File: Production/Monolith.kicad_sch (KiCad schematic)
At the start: 0 parts

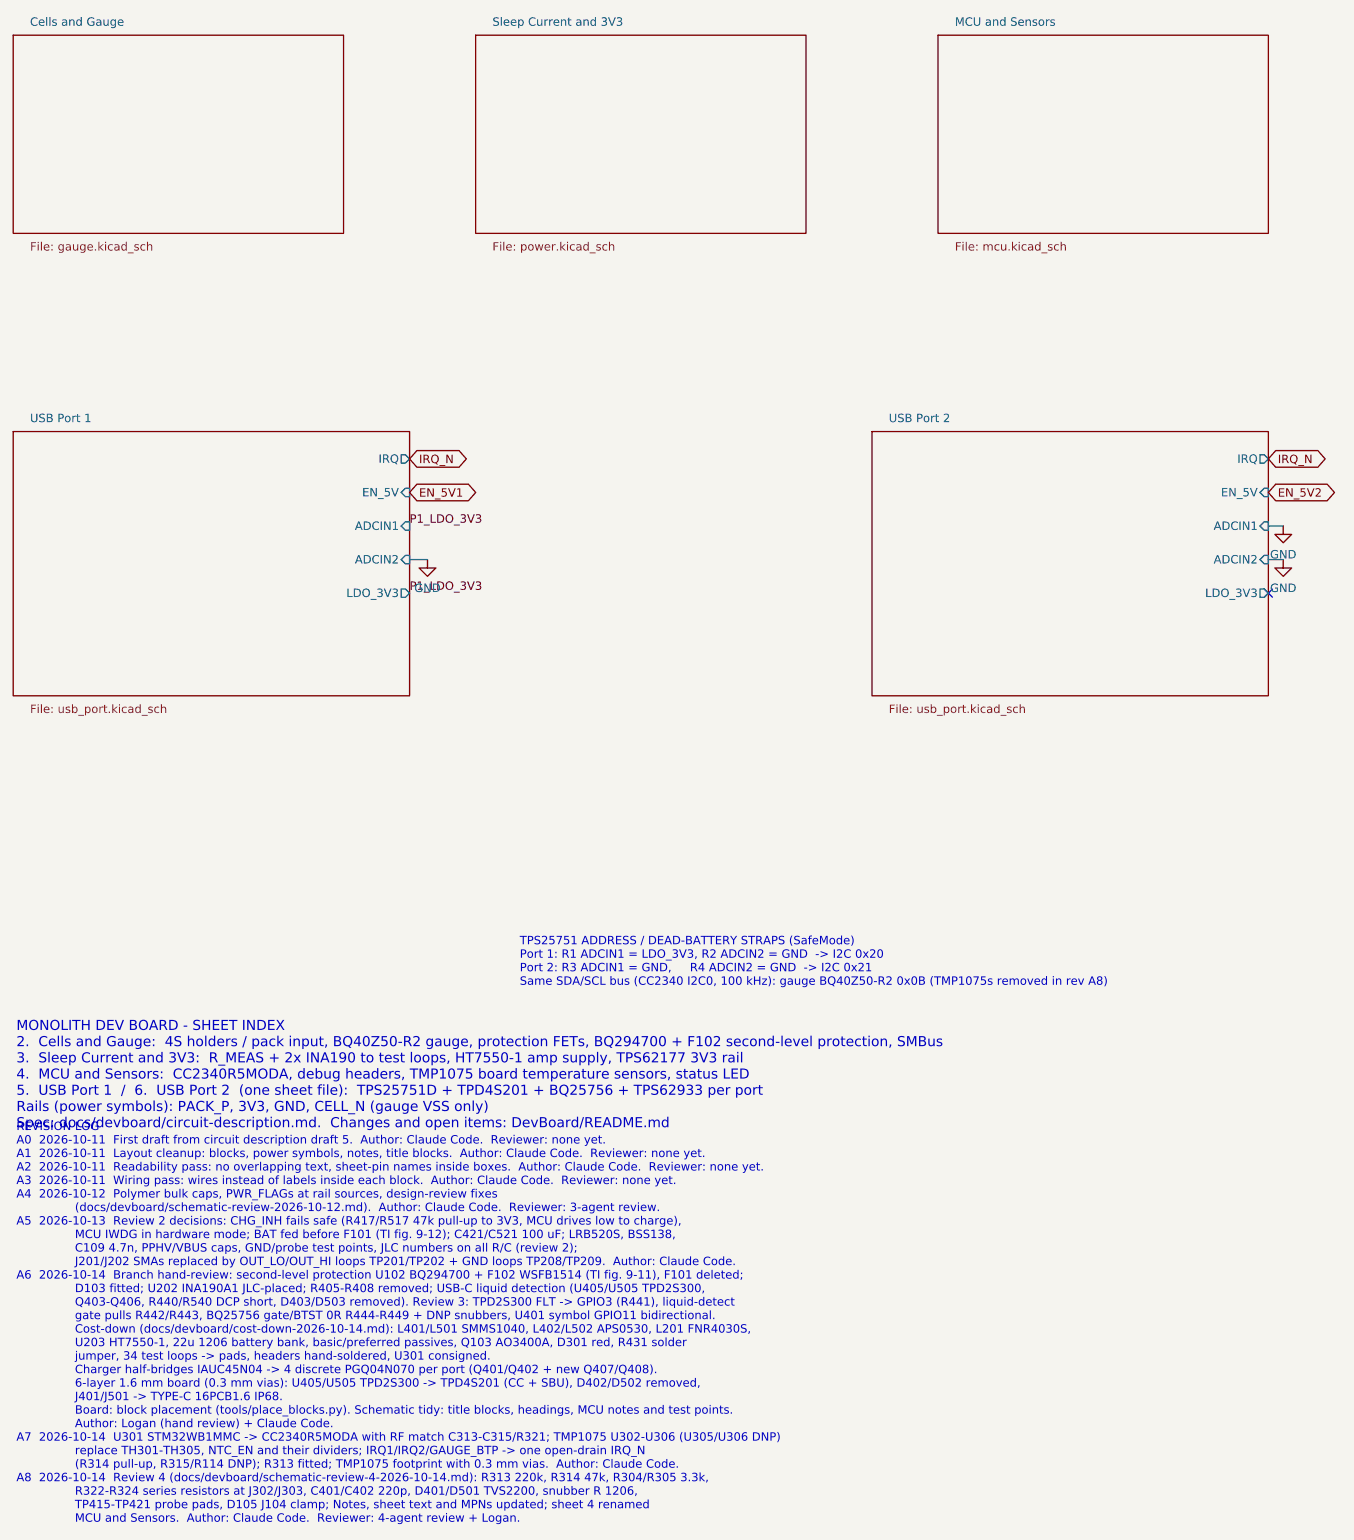
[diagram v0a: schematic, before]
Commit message: Production schematic P0: drawing tidy
tools/tidy_production.py (runs after make_production.py): pogo pads in their
own row, TC2030 under its SWD heading, link-merge leftovers removed, empty
headings deleted, sheet notes, root index and revision log rewritten for
production, sheets renamed 3V3 Rail and MCU. Netlist unchanged (check_netlist
passes); ERC: no errors.

Co-Authored-By: Claude Opus 5.5 <noreply@anthropic.com>
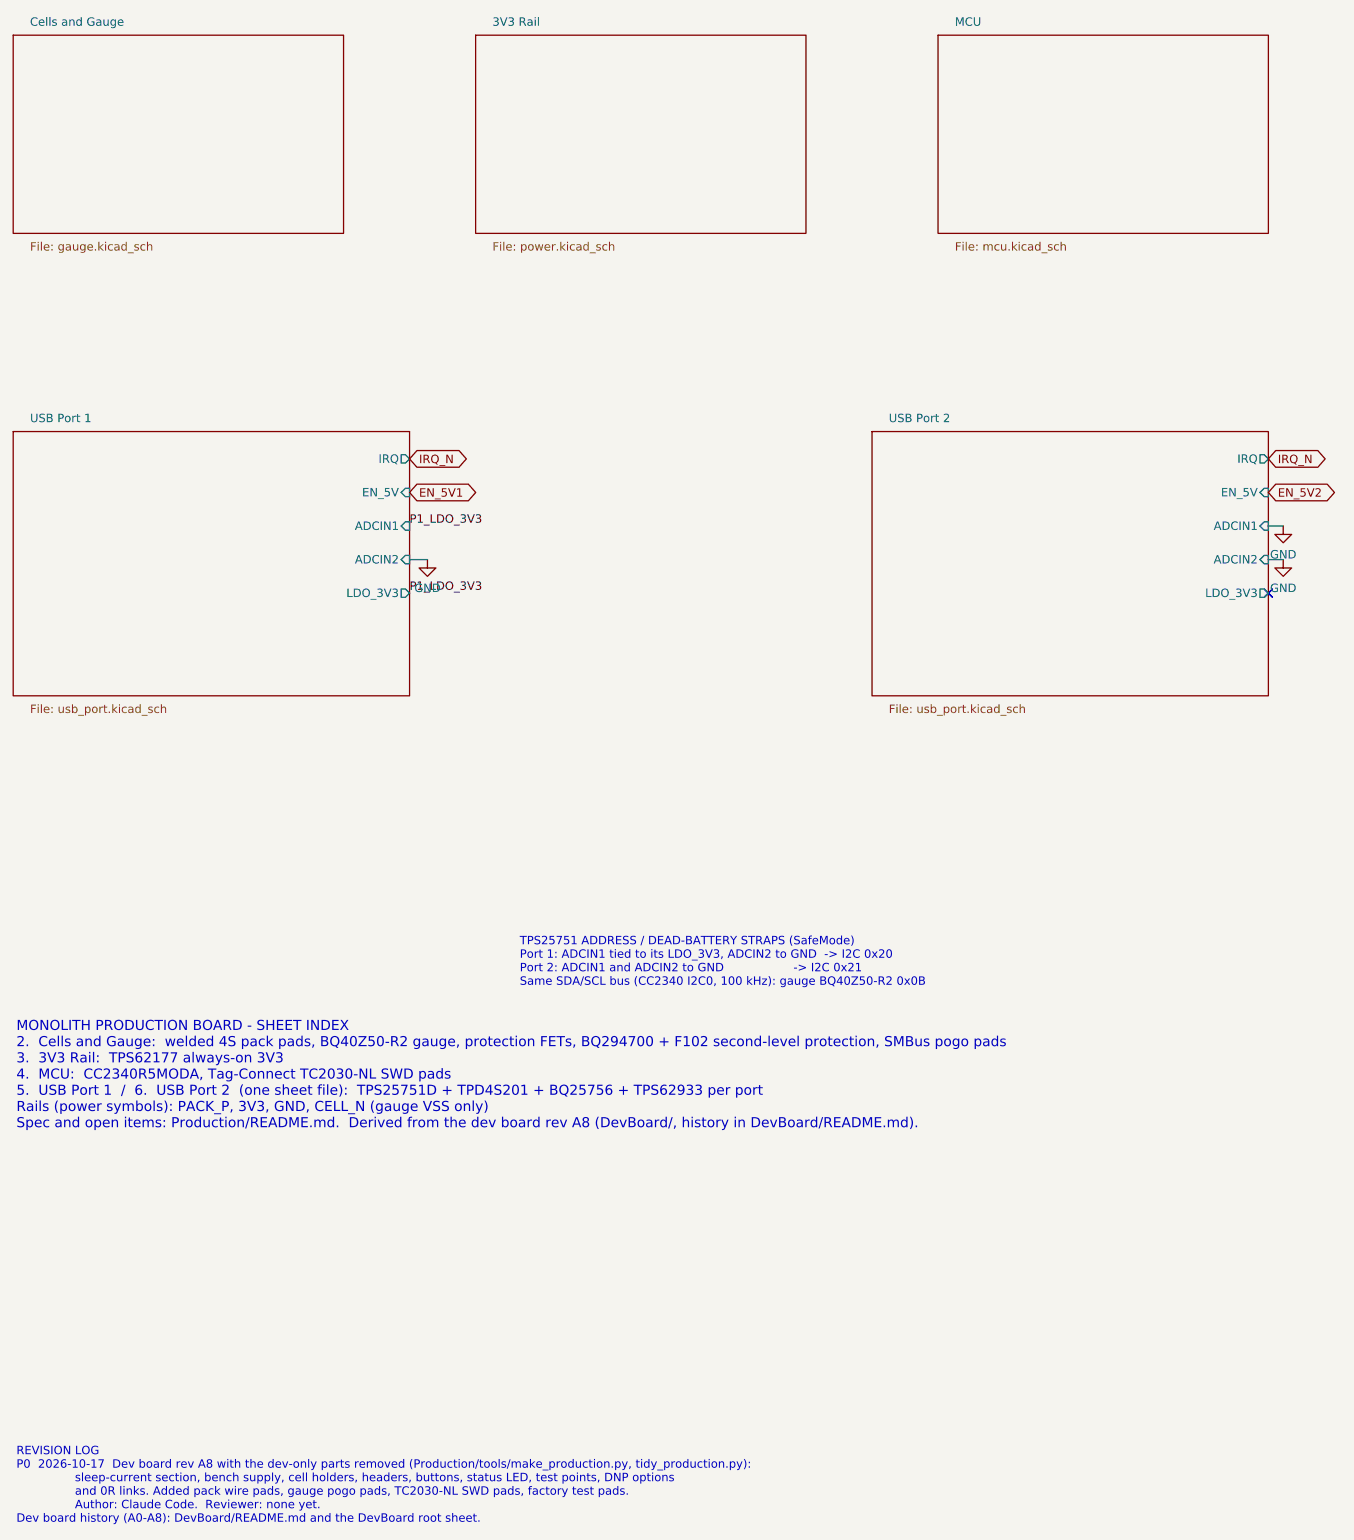
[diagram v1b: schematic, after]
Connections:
- no-connect marks 1 -> 2
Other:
- sheet MCU and Sensors renamed MCU
- sheet Sleep Current and 3V3 renamed 3V3 Rail
- note added: "MONOLITH PRODUCTION BOARD - SHEET INDEX 2. Cells and Gauge: welded 4S pack pads, BQ40Z50-R2 gauge, protection FETs, BQ294700 + F102 second-level protection, SMBus pogo pads 3. 3V3 Rail: TPS62177 always-on 3V3 4. MCU: CC2340R5MODA, Tag-Connect TC2030-NL SWD pads 5. USB Port 1 / 6. USB Port 2 (one sheet file): TPS25751D + TPD4S201 + BQ25756 + TPS62933 per port Rails (power symbols): PACK_P, 3V3, GN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"
- note added: "REVISION LOG P0 2026-10-17 Dev board rev A8 with the dev-only parts removed (Production/tools/make_production.py, tidy_production.py): sleep-current section, bench supply, cell holders, headers, buttons, status LED, test points, DNP options and 0R links. Added pack wire pads, gauge pogo pads, TC2030-NL SWD pads, factory test pads. Author: Claude Code. Reviewer: none yet. Dev board history (A0-A8)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"
- note added: "TPS25751 ADDRESS / DEAD-BATTERY STRAPS (SafeMode) Port 1: ADCIN1 tied to its LDO_3V3, ADCIN2 to GND -> I2C 0x20 Port 2: ADCIN1 and ADCIN2 to GND -> I2C 0x21 Same SDA/SCL bus (CC2340 I2C0, 100 kHz): gauge BQ40Z50-R2 0x0B"
- note removed: "MONOLITH DEV BOARD - SHEET INDEX 2. Cells and Gauge: 4S holders / pack input, BQ40Z50-R2 gauge, protection FETs, BQ294700 + F102 second-level protection, SMBus 3. Sleep Current and 3V3: R_MEAS + 2x INA190 to test loops, HT7550-1 amp supply, TPS62177 3V3 rail 4. MCU and Sensors: CC2340R5MODA, debug headers, TMP1075 board temperature sensors, status LED 5. USB Port 1 / 6. USB Port 2 (one sheet file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"
- note removed: "REVISION LOG A0 2026-10-11 First draft from circuit description draft 5. Author: Claude Code. Reviewer: none yet. A1 2026-10-11 Layout cleanup: blocks, power symbols, notes, title blocks. Author: Claude Code. Reviewer: none yet. A2 2026-10-11 Readability pass: no overlapping text, sheet-pin names inside boxes. Author: Claude Code. Reviewer: none yet. A3 2026-10-11 Wiring pass: wires instead of la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"
- note removed: "TPS25751 ADDRESS / DEAD-BATTERY STRAPS (SafeMode) Port 1: R1 ADCIN1 = LDO_3V3, R2 ADCIN2 = GND -> I2C 0x20 Port 2: R3 ADCIN1 = GND, R4 ADCIN2 = GND -> I2C 0x21 Same SDA/SCL bus (CC2340 I2C0, 100 kHz): gauge BQ40Z50-R2 0x0B (TMP1075s removed in rev A8)"
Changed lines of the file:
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@@
 		(company "Monolith 100 W battery bank - production")
 		(comment 1 "Sheet index, PD address straps")
-		(comment 2 "Spec + open items: DevBoard/README.md")
+		(comment 2 "Spec + open items: Production/README.md")
 		(comment 3 "P0: dev board rev A8 stripped by Production/tools/make_production.py; not reviewed")
 	)
-	(text "MONOLITH DEV BOARD - SHEET INDEX\n2.  Cells and Gauge:  4S holders / pack input, BQ40Z50-R2 gauge, protection FETs, BQ294700 + F102 second-level protection, SMBus\n3.  Sleep Current and 3V3:  R_MEAS + 2x INA190 to test loops, HT7550-1 amp supply, TPS62177 3V3 rail\n4.  MCU and Sensors:  CC2340R5MODA, debug headers, TMP1075 board temperature sensors, status LED\n5.  USB Port 1  /  6.  USB Port 2  (one sheet file):  TPS25751D + TPD4S201 + BQ25756 + TPS62933 per port\nRails (power symbols): PACK_P, 3V3, GND, CELL_N (gauge VSS only)\nSpec: docs/devboard/circuit-description.md.  Changes and open items: DevBoard/README.md"
+	(text "MONOLITH PRODUCTION BOARD - SHEET INDEX\n2.  Cells and Gauge:  welded 4S pack pads, BQ40Z50-R2 gauge, protection FETs, BQ294700 + F102 second-level protection, SMBus pogo pads\n3.  3V3 Rail:  TPS62177 always-on 3V3\n4.  MCU:  CC2340R5MODA, Tag-Connect TC2030-NL SWD pads\n5.  USB Port 1  /  6.  USB Port 2  (one sheet file):  TPS25751D + TPD4S201 + BQ25756 + TPS62933 per port\nRails (power symbols): PACK_P, 3V3, GND, CELL_N (gauge VSS only)\nSpec and open items: Production/README.md.  Derived from the dev board rev A8 (DevBoard/, history in DevBoard/README.md)."
 		(exclude_from_sim no)
 		(at 30.48 205.74 0)
@@
 		)
 	)
-	(text "REVISION LOG\nA0  2026-10-11  First draft from circuit description draft 5.  Author: Claude Code.  Reviewer: none yet.\nA1  2026-10-11  Layout cleanup: blocks, power symbols, notes, title blocks.  Author: Claude Code.  Reviewer: none yet.\nA2  2026-10-11  Readability pass: no overlapping text, sheet-pin names inside boxes.  Author: Claude Code.  Reviewer: none yet.\nA3  2026-10-11  Wiring pass: wires instead of labels inside each block.  Author: Claude Code.  Reviewer: none yet.\nA4  2026-10-12  Polymer bulk caps, PWR_FLAGs at rail sources, design-review fixes\n                (docs/devboard/schematic-review-2026-10-12.md).  Author: Claude Code.  Reviewer: 3-agent review.\nA5  2026-10-13  Review 2 decisions: CHG_INH fails safe (R417/R517 47k pull-up to 3V3, MCU drives low to charge),\n                MCU IWDG in hardware mode; BAT fed before F101 (TI fig. 9-12); C421/C521 100 uF; LRB520S, BSS138,\n                C109 4.7n, PPHV/VBUS caps, GND/probe test points, JLC numbers on all R/C (review 2);\n                J201/J202 SMAs replaced by OUT_LO/OUT_HI loops TP201/TP202 + GND loops TP208/TP209.  Author: Claude Code.\nA6  2026-10-14  Branch hand-review: second-level protection U102 BQ294700 + F102 WSFB1514 (TI fig. 9-11), F101 deleted;\n                D103 fitted; U202 INA190A1 JLC-placed; R405-R408 removed; USB-C liquid detection (U405/U505 TPD2S300,\n                Q403-Q406, R440/R540 DCP short, D403/D503 removed). Review 3: TPD2S300 FLT -> GPIO3 (R441), liquid-detect\n                gate pulls R442/R443, BQ25756 gate/BTST 0R R444-R449 + DNP snubbers, U401 symbol GPIO11 bidirectional.\n                Cost-down (docs/devboard/cost-down-2026-10-14.md): L401/L501 SMMS1040, L402/L502 APS0530, L201 FNR4030S,\n                U203 HT7550-1, 22u 1206 battery bank, basic/preferred passives, Q103 AO3400A, D301 red, R431 solder\n                jumper, 34 test loops -> pads, headers hand-soldered, U301 consigned.\n                Charger half-bridges IAUC45N04 -> 4 discrete PGQ04N070 per port (Q401/Q402 + new Q407/Q408).\n                6-layer 1.6 mm board (0.3 mm vias): U405/U505 TPD2S300 -> TPD4S201 (CC + SBU), D402/D502 removed,\n                J401/J501 -> TYPE-C 16PCB1.6 IP68.\n                Board: block placement (tools/place_blocks.py). Schematic tidy: title blocks, headings, MCU notes and test points.\n                Author: Logan (hand review) + Claude Code.\nA7  2026-10-14  U301 STM32WB1MMC -> CC2340R5MODA with RF match C313-C315/R321; TMP1075 U302-U306 (U305/U306 DNP)\n                replace TH301-TH305, NTC_EN and their dividers; IRQ1/IRQ2/GAUGE_BTP -> one open-drain IRQ_N\n                (R314 pull-up, R315/R114 DNP); R313 fitted; TMP1075 footprint with 0.3 mm vias.  Author: Claude Code.\nA8  2026-10-14  Review 4 (docs/devboard/schematic-review-4-2026-10-14.md): R313 220k, R314 47k, R304/R305 3.3k,\n                R322-R324 series resistors at J302/J303, C401/C402 220p, D401/D501 TVS2200, snubber R 1206,\n                TP415-TP421 probe pads, D105 J104 clamp; Notes, sheet text and MPNs updated; sheet 4 renamed\n                MCU and Sensors.  Author: Claude Code.  Reviewer: 4-agent review + Logan."
+	(text "REVISION LOG\nP0  2026-10-17  Dev board rev A8 with the dev-only parts removed (Production/tools/make_production.py, tidy_production.py):\n                sleep-current section, bench supply, cell holders, headers, buttons, status LED, test points, DNP options\n                and 0R links. Added pack wire pads, gauge pogo pads, TC2030-NL SWD pads, factory test pads.\n                Author: Claude Code.  Reviewer: none yet.\nDev board history (A0-A8): DevBoard/README.md and the DevBoard root sheet."
 		(exclude_from_sim no)
 		(at 30.48 265.43 0)
@@
 		)
 	)
-	(text "TPS25751 ADDRESS / DEAD-BATTERY STRAPS (SafeMode)\nPort 1: R1 ADCIN1 = LDO_3V3, R2 ADCIN2 = GND  -> I2C 0x20\nPort 2: R3 ADCIN1 = GND,     R4 ADCIN2 = GND  -> I2C 0x21\nSame SDA/SCL bus (CC2340 I2C0, 100 kHz): gauge BQ40Z50-R2 0x0B (TMP1075s removed in rev A8)"
+	(text "TPS25751 ADDRESS / DEAD-BATTERY STRAPS (SafeMode)\nPort 1: ADCIN1 tied to its LDO_3V3, ADCIN2 to GND  -> I2C 0x20\nPort 2: ADCIN1 and ADCIN2 to GND                   -> I2C 0x21\nSame SDA/SCL bus (CC2340 I2C0, 100 kHz): gauge BQ40Z50-R2 0x0B"
 		(exclude_from_sim no)
 		(at 106.68 184.15 0)
@@
 			(justify left bottom)
 		)
+	)
+	(no_connect
+		(at 220 124.46)
 	)
 	(label "P1_LDO_3V3"
@@
 			(color 0 0 0 0)
 		)
-		(property "Sheetname" "MCU and Sensors"
+		(property "Sheetname" "MCU"
 			(at 172.54 38.73 0)
 			(show_name no)
@@
 			(color 0 0 0 0)
 		)
-		(property "Sheetname" "Sleep Current and 3V3"
+		(property "Sheetname" "3V3 Rail"
 			(at 102.54 38.73 0)
 			(show_name no)
